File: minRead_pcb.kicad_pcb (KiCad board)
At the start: 2 copper layers, 60 x 111.3 mm, 170 parts, among them J1 USB_C_Receptacle, J2 FH34SRJ-24S-0.5SH_50_, J3 FH34SRJ-6S-0.5SH_50_, J4 FH34SRJ-6S-0.5SH_50_, J5 Conn_01x02, J6 PPPC062LJBN-RC, J7 Micro_SD_Card, Q1 FS8205A, Q12 MMBT3904, Q13 MMBT3904, Q14 AO3419, Q15 MMBT3906, Q3 AO3419, Q4 BSS138, Q5 BSS138, Q6 BSS138, Q7 AO3419, Q8 AO3419, Q9 BSS138, SW1 SW_Push, SW10 SW_Push, SW11 SW_Push, SW2 SW_Push, SW3 SW_Push, SW4 SW_Push, SW5 SW_Push, SW6 SW_Push, SW7 SW_Push, SW8 SW_Push, SW9 SW_Push, U1 TPD4E1U06DBVR, U10 AP3031KTR, U11 TP4056-42-ESOP8, U12 74LVC1G04, U13 DS3231MZ, U2 TPS2116DRL, U3 AP2112K-3.3, U4 ESP32-S3-WROOM-1, U5 DW01A, U6 TPD4E1U06DBVR, U7 TPD4E1U06DBVR, U8 TPD4E1U06DBVR, U9 TPD4E1U06DBVR

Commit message: added voltage divider to 3031 reduced led driver passives size to 0603
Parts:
- added R66: 680k, Resistor_SMD:R_0603_1608Metric_Pad0.98x0.95mm_HandSolder, B.Cu at (58.0, 134.0)
- added R67: 1M, Resistor_SMD:R_0603_1608Metric_Pad0.98x0.95mm_HandSolder, B.Cu at (58.0, 135.5)
- C12, C21, C23, C24: footprint Capacitor_SMD:C_0805_2012Metric_Pad1.18x1.45mm_HandSolder -> Capacitor_SMD:C_0603_1608Metric_Pad1.08x0.95mm_HandSolder
- R17, R37, R39, R40, R41, R42, R43, R44, R45, R46, R49, R50, R52: footprint Resistor_SMD:R_0805_2012Metric_Pad1.20x1.40mm_HandSolder -> Resistor_SMD:R_0603_1608Metric_Pad0.98x0.95mm_HandSolder
- moved R41 1.44 mm to (58.0, 132.5), turned to 180 degrees
- moved C9 0.77 mm to (57.7, 137.3), turned to 0 degrees
- moved D9 0.24 mm to (58.3, 129.5)
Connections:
- U10 pad 5: LED_SW -> /OVP
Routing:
- net LED_SW: track 180.8 -> 171.4 mm
- net /OVP: track 0.00 -> 7.81 mm
- net Net-(Q5-S): track 40.1 -> 41.9 mm
- net GND: vias 48 -> 53

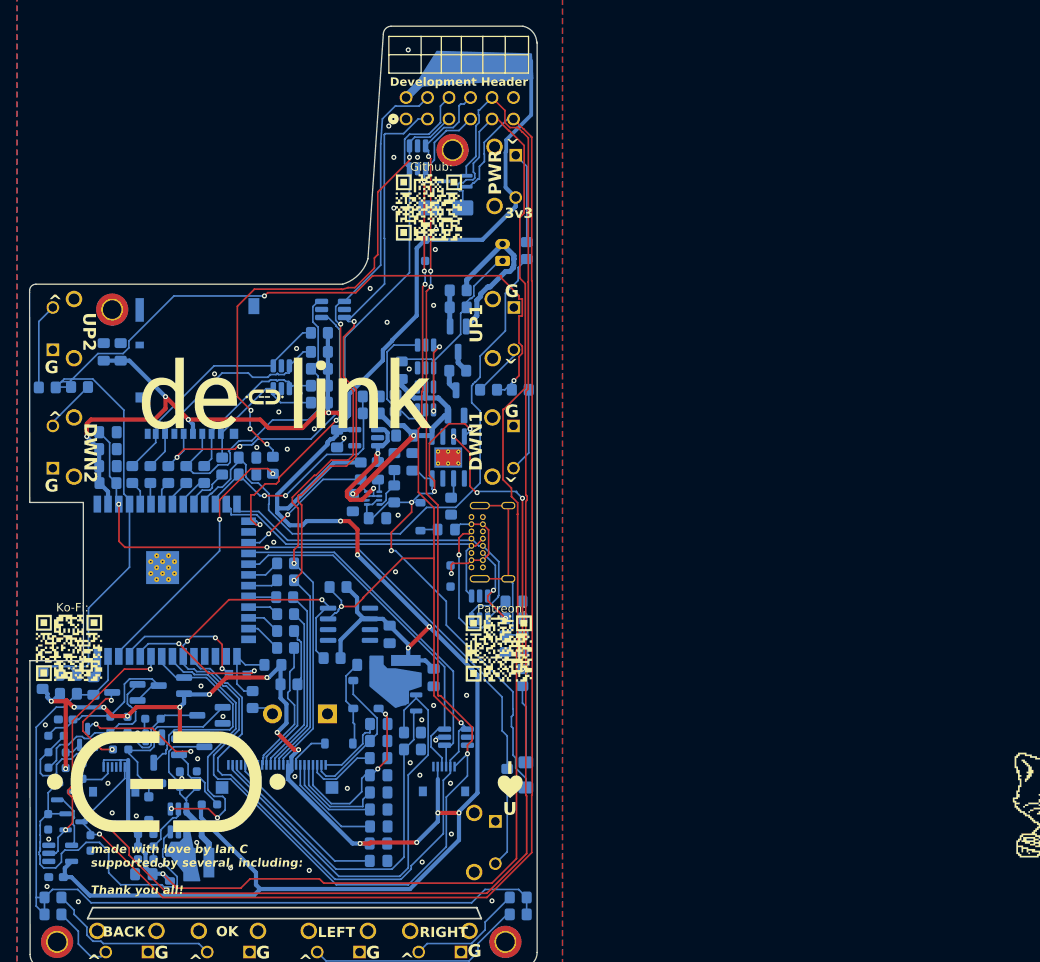
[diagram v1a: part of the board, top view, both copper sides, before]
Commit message: updated silkscreen reference spacing updated silkscreen of graphics still need to do more of above added netclass for switching nodes and high voltage output caps, enforced 3mm clearance
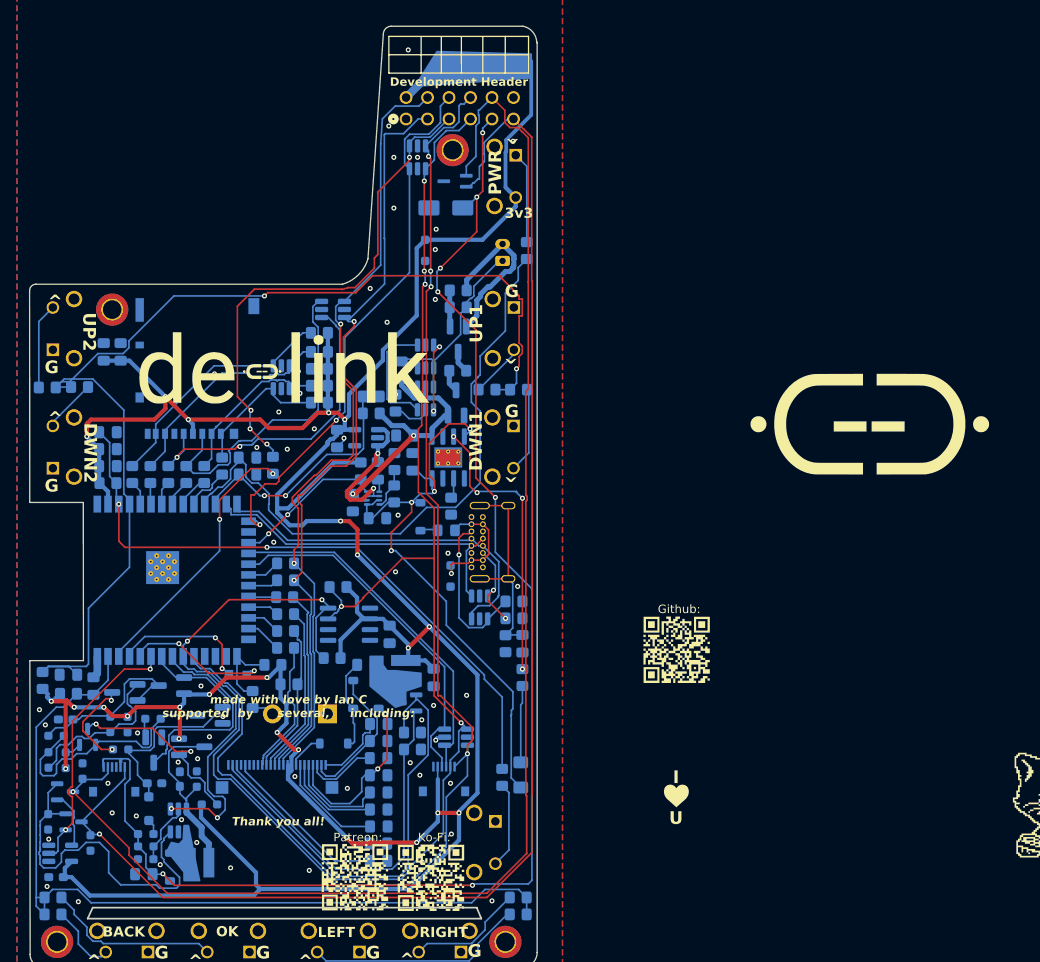
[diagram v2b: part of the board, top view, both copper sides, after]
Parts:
- removed the G*** at (123.8, 33.0)
- moved G*** 93.3 mm to (143.5, 84.1)
- moved G*** 59.9 mm to (120.7, 110.7)
- moved G*** 50.7 mm to (91.7, 137.7)
- moved G*** 31.9 mm to (82.7, 137.6)
- moved G*** 19.7 mm to (120.7, 128.0)
- moved G*** 3.02 mm to (74.1, 77.8)
- moved D2 0.60 mm to (102.3, 125.5)
- moved R63 0.60 mm to (100.1, 125.8)
- moved D6 0.60 mm to (80.2, 121.8)
- moved R61 0.20 mm to (102.0, 80.0)
- moved R11 0.18 mm to (98.3, 80.0)
- moved F1 0.10 mm to (93.5, 96.6)
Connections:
- net /3031_SW renamed 3031_SW
- net Net-(D5-A) renamed EINK_SW
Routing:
- net LED_SW: track 171.4 -> 166.8 mm, vias 1 -> 7
- net 3V3: track 411.3 -> 413.2 mm
- net Net-(Q5-S): track 41.9 -> 42.6 mm
- net Net-(D4-K): track 10.3 -> 10.9 mm
- net GND: track 11.8 -> 11.2 mm, vias 53 -> 57
- net 3031_SW: track 0.55 -> 0.00 mm
- net (no net): vias 0 -> 1
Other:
- board text added: "Thank you all!"
- board text added: "made with love by Ian C supported by several, including:"
- board text removed: "EPaper Connector"
- board text removed: "LED"
- board text removed: "made with love by Ian C supported by several, including: Thank you all!"
